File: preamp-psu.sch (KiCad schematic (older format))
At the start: 34 parts

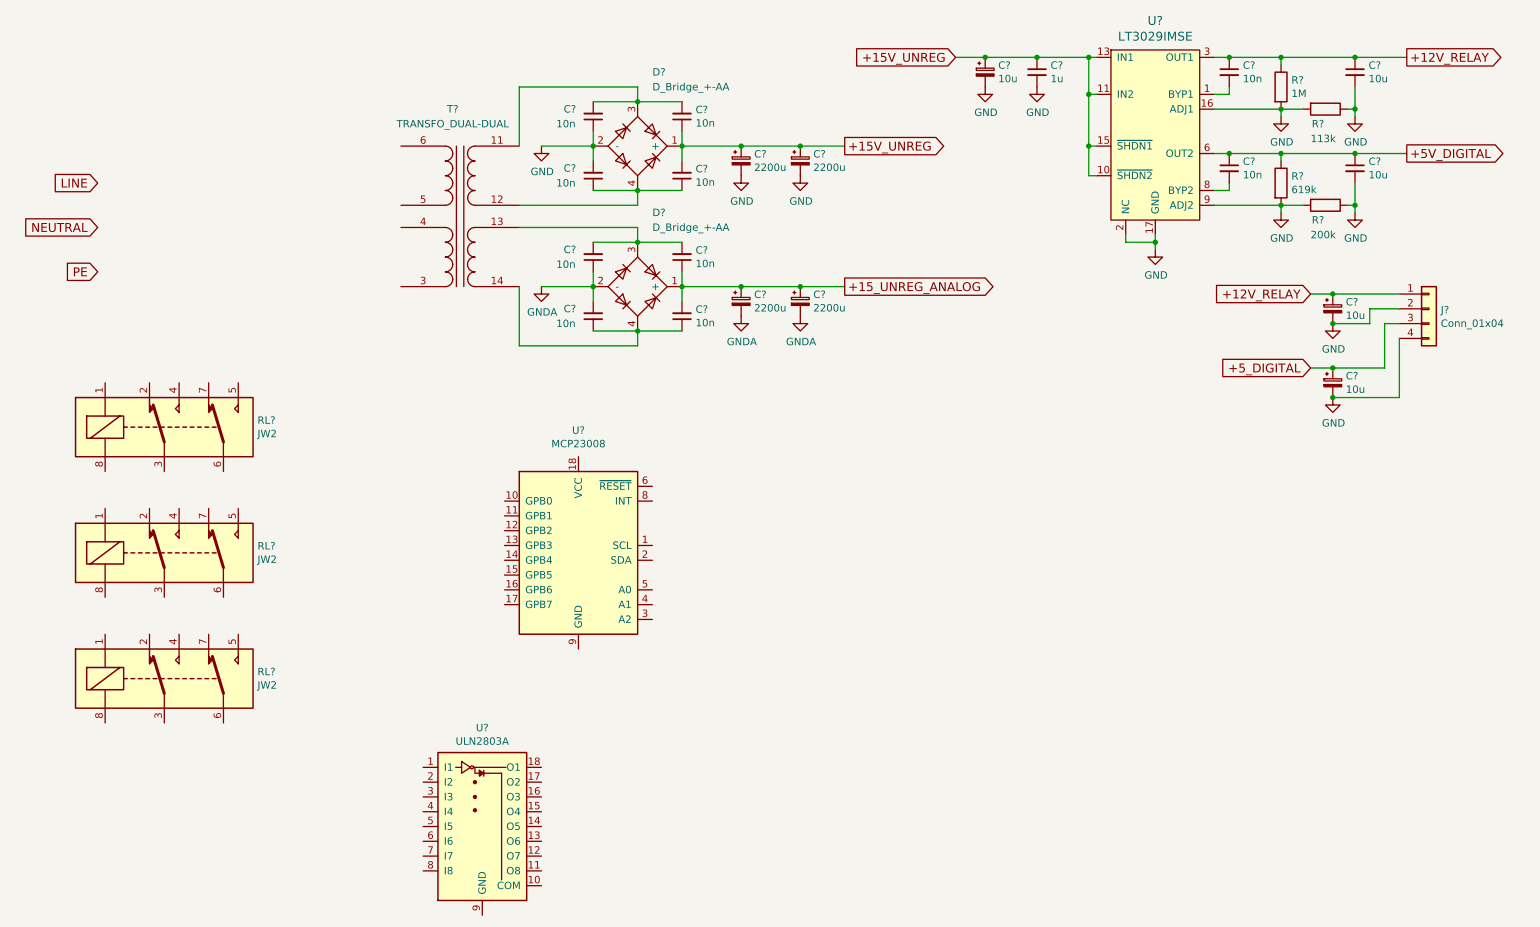
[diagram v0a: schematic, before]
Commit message: add lt3045
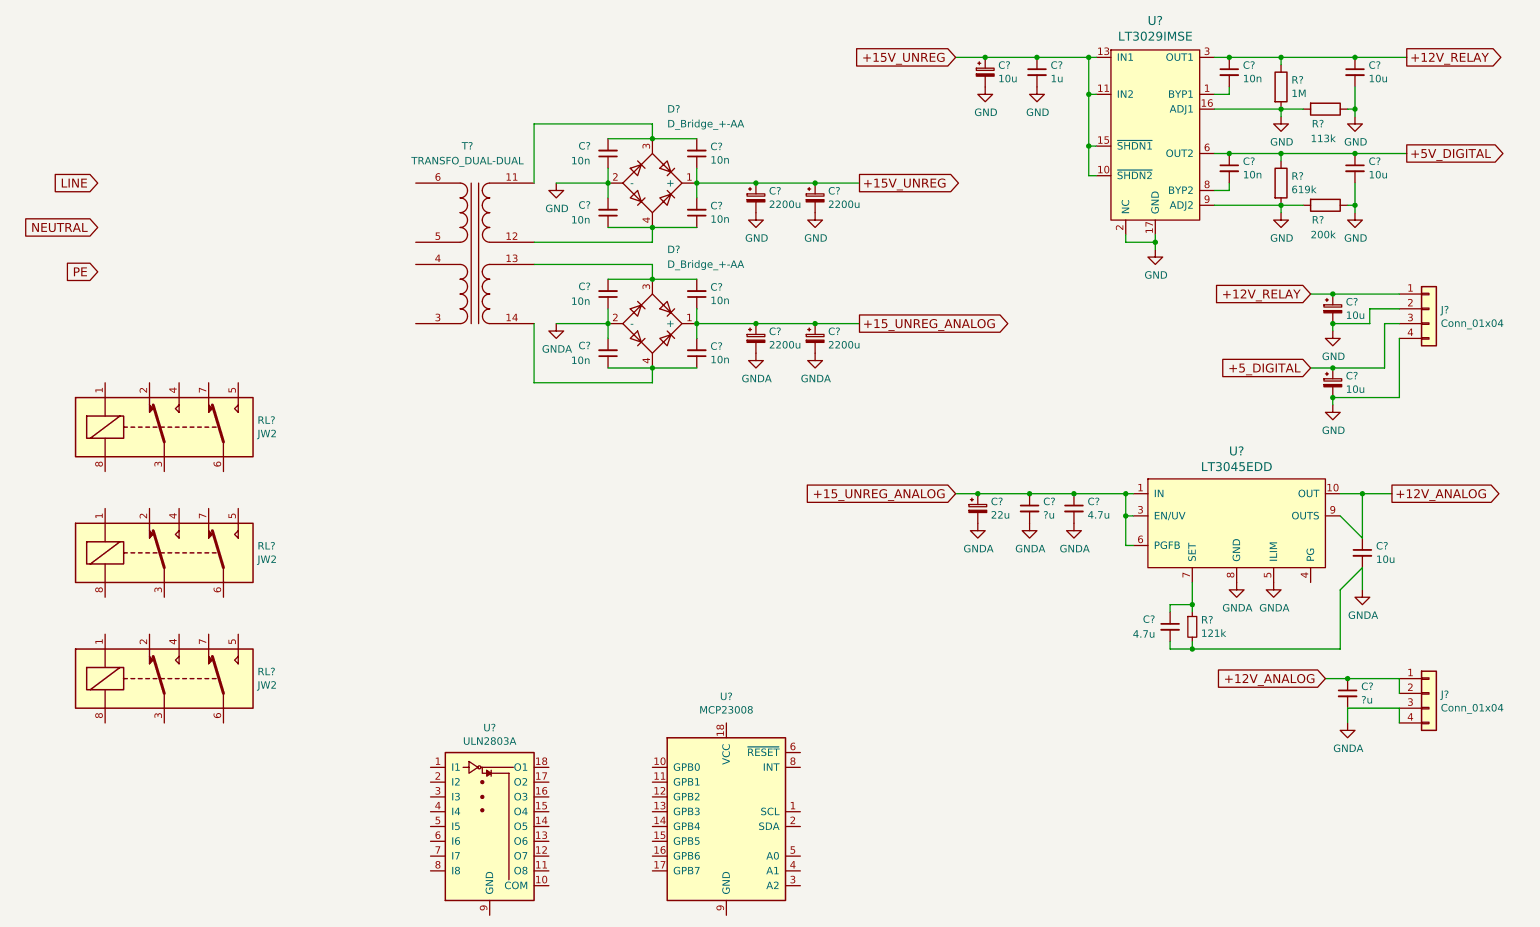
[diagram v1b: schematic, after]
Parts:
- added C? (x2): 4.7u, symbol C_Small
- added C?: 22u, symbol CP_Small
- added C? (x2): ?u, symbol C_Small
- added C?: 10u, symbol C_Small
- added J?: Conn_01x04, symbol Conn_01x04
- added R?: 121k, symbol R_Small
- added U?: LT3045EDD, Housings_DFN_QFN:DFN-10-1EP_3x3mm_Pitch0.5mm, symbol LT3045EDD
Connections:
- net +15_UNREG_ANALOG: now also C?.1, C?.1, C?.1, U?.1 (IN), U?.3 (EN/UV), U?.6 (PGFB)
- net GNDA: now also C?.2, C?.2, C?.2, C?.2, C?.2, C?.2, J?.3 (Pin_3), J?.4 (Pin_4), R?.2, U?.5 (ILIM), U?.8 (GND)
- new net: C?.1, R?.1, U?.7 (SET)
- new net +12V_ANALOG: C?.1, C?.1, J?.1 (Pin_1), J?.2 (Pin_2), U?.10 (OUT), U?.9 (OUTS)
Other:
- moved on the sheet: C?, D?, T?, U?
